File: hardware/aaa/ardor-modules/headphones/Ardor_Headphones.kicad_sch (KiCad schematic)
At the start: 21 parts, among them J101 +5V / GND / HP_ENABLE, J102 AUDIO_L / GND / AUDIO_R, J602 HP_L / HP_R / GND, U601 TPA6132A2RTER

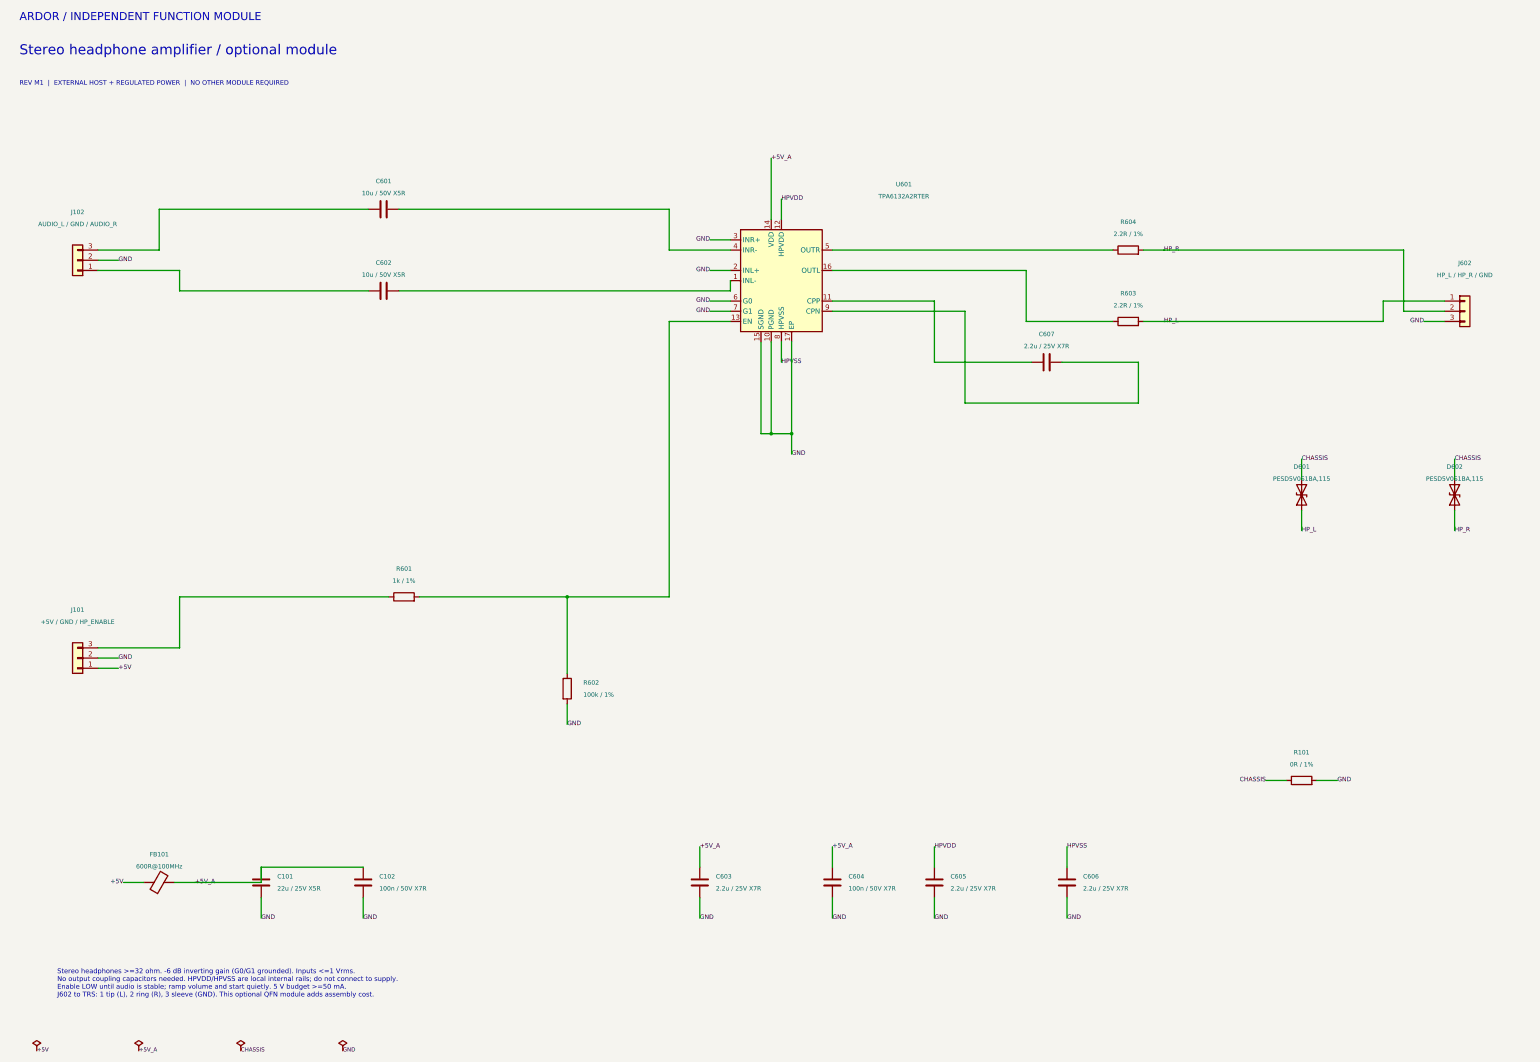
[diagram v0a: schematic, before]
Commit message: feat: clarify module pin labels and add STE assembly guides
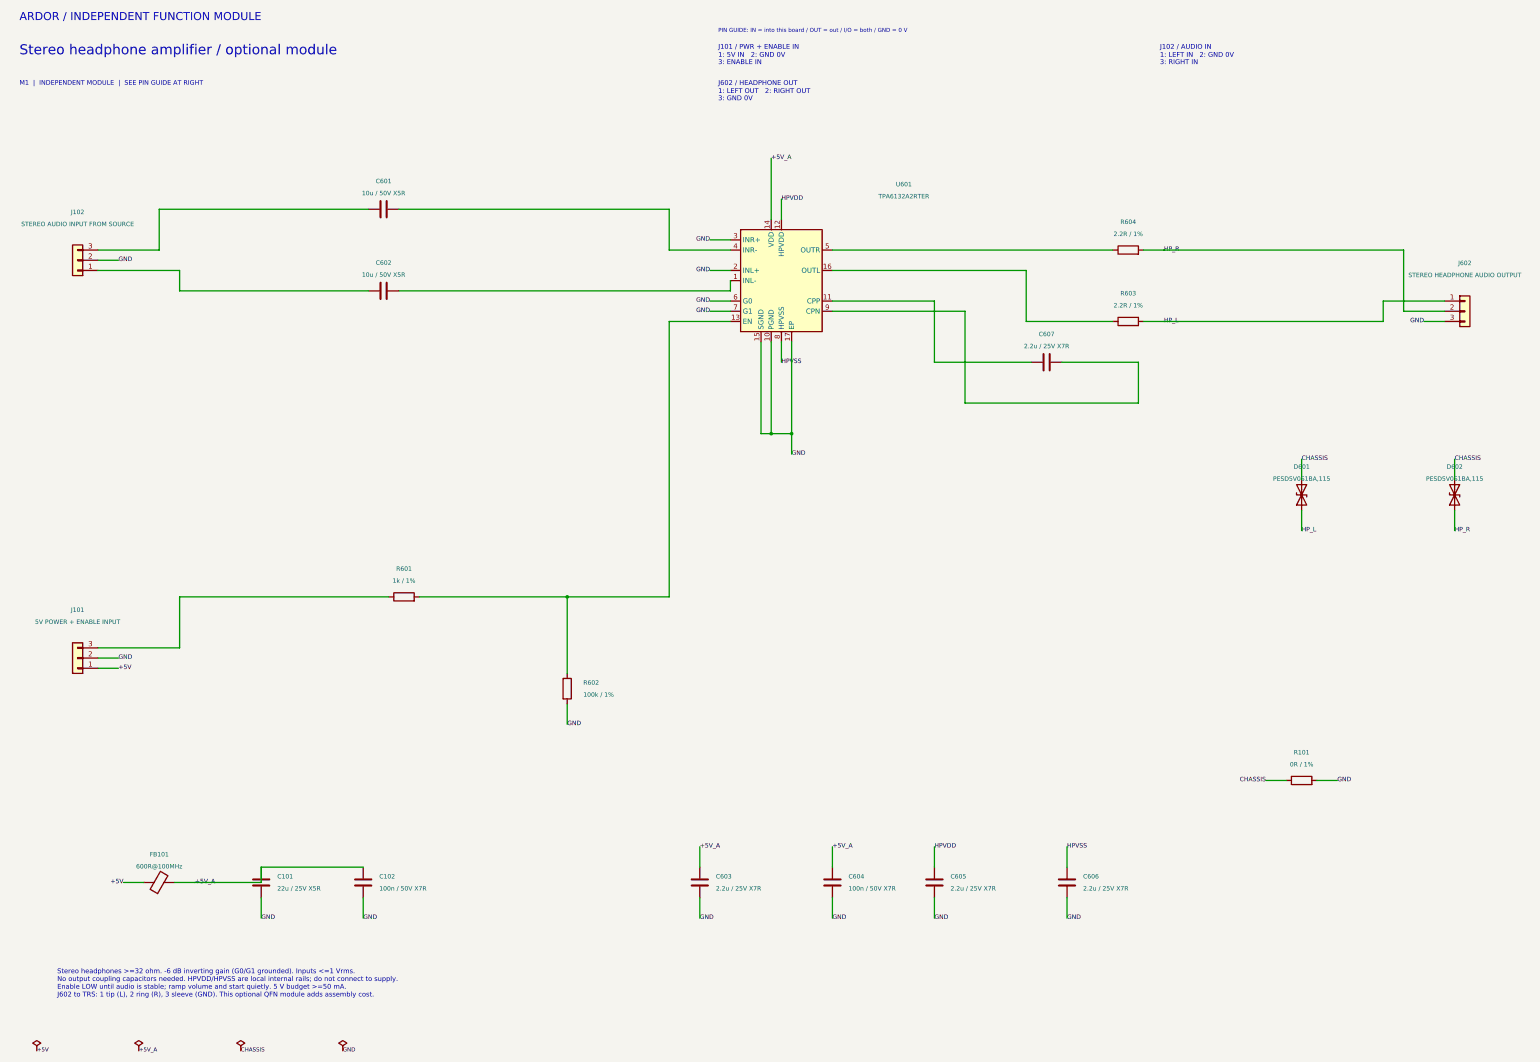
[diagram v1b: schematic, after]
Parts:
- J101: value +5V / GND / HP_ENABLE -> 5V POWER + ENABLE INPUT
- J102: value AUDIO_L / GND / AUDIO_R -> STEREO AUDIO INPUT FROM SOURCE
- J602: value HP_L / HP_R / GND -> STEREO HEADPHONE AUDIO OUTPUT
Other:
- note added: "1: 5V IN 2: GND 0V"
- note added: "1: LEFT IN 2: GND 0V"
- note added: "1: LEFT OUT 2: RIGHT OUT"
- note added: "3: ENABLE IN"
- note added: "3: GND 0V"
- note added: "3: RIGHT IN"
- note added: "J101 / PWR + ENABLE IN"
- note added: "J102 / AUDIO IN"
- note added: "J602 / HEADPHONE OUT"
- note added: "M1 | INDEPENDENT MODULE | SEE PIN GUIDE AT RIGHT"
- note added: "PIN GUIDE: IN = into this board / OUT = out / I/O = both / GND = 0 V"
- note removed: "REV M1 | EXTERNAL HOST + REGULATED POWER | NO OTHER MODULE REQUIRED"
